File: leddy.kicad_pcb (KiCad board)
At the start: 2 copper layers, 10 parts

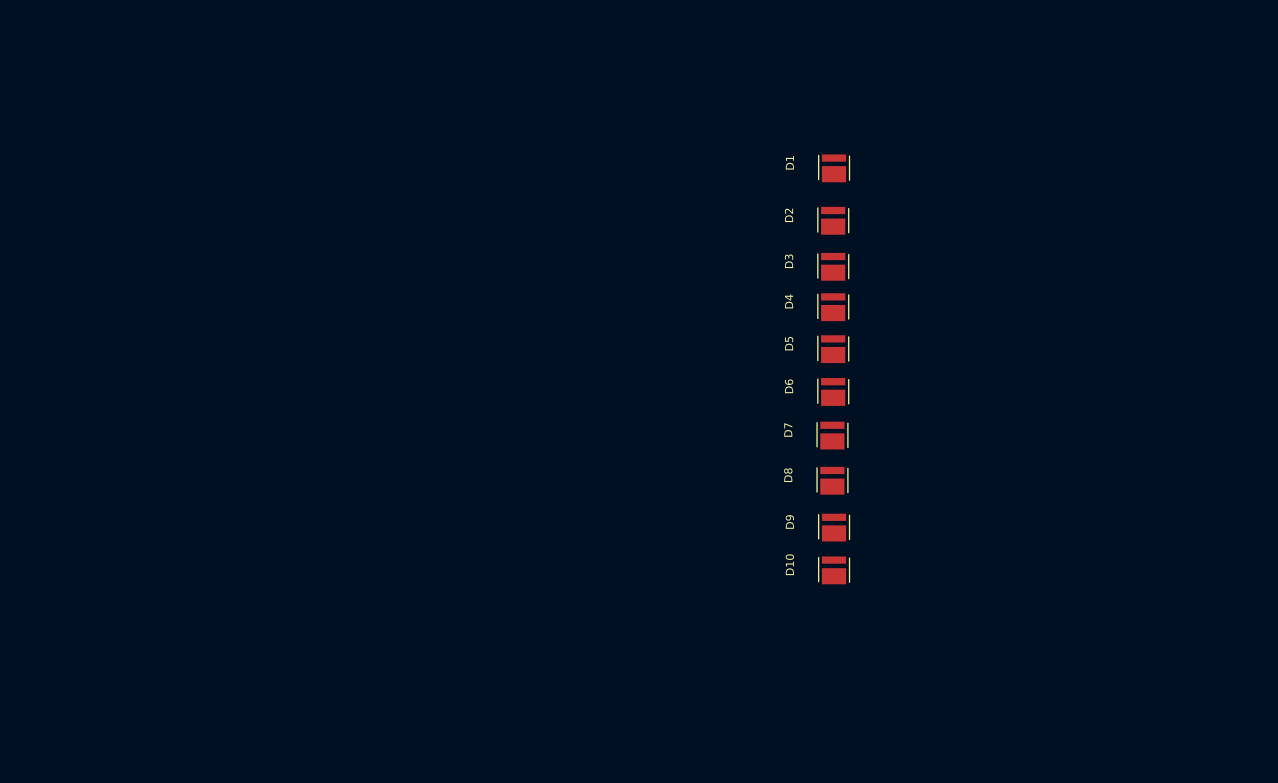
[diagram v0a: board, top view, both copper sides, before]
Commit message: added LED driver IC and added a total of 50 LEDs
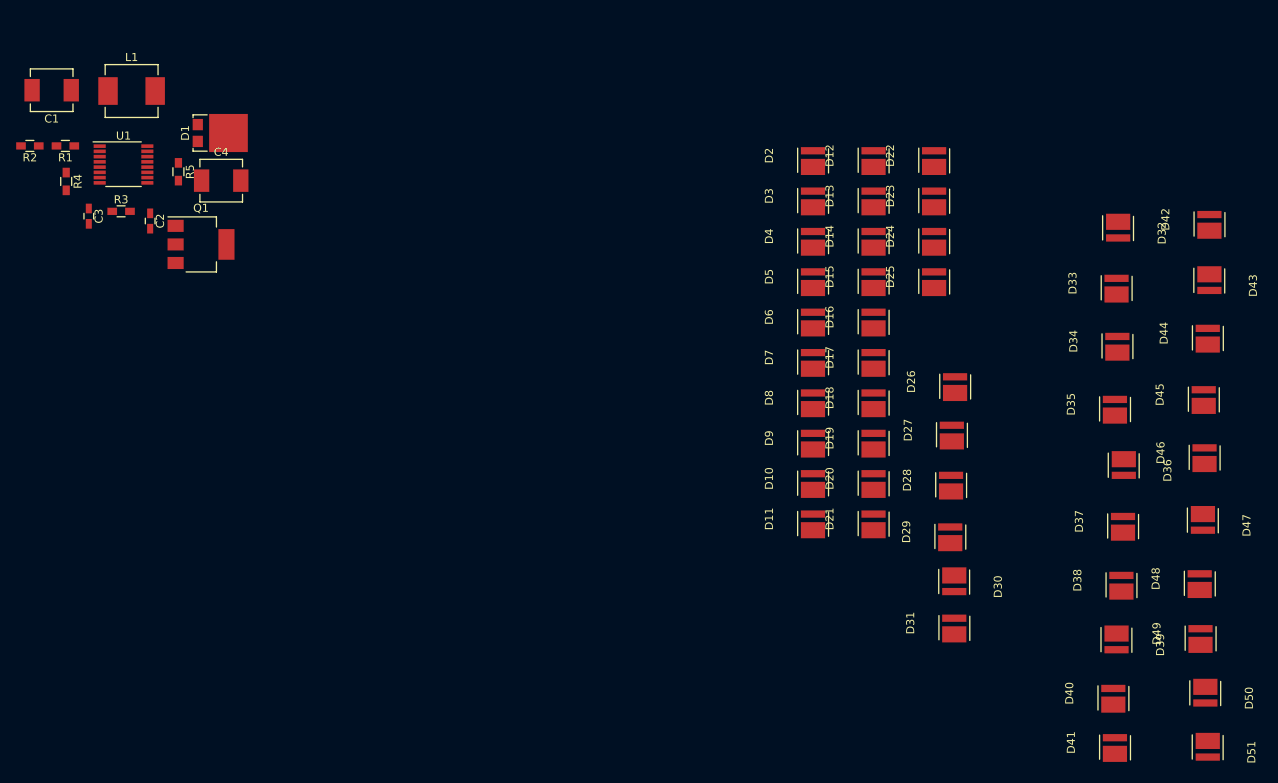
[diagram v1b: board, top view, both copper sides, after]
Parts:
- added C1: 10uF, Inductors_SMD:L_Vishay_IHLP-2020, F.Cu at (70.7, 54.1)
- added C2: 0.1uF, Capacitors_SMD:C_0603_HandSoldering, F.Cu at (82.9, 70.3)
- added C3: 0.1uF, Capacitors_SMD:C_0603_HandSoldering, F.Cu at (75.3, 69.7)
- added C4: 10uF, Inductors_SMD:L_Vishay_IHLP-2020, F.Cu at (91.7, 65.3)
- added D11: LED, lib:LED-3030, F.Cu at (165.0, 107.5)
- added D12: LED, lib:LED-3030, F.Cu at (172.5, 62.5)
- added D13: LED, lib:LED-3030, F.Cu at (172.5, 67.5)
- added D14: LED, lib:LED-3030, F.Cu at (172.5, 72.5)
- added D15: LED, lib:LED-3030, F.Cu at (172.5, 77.5)
- added D16: LED, lib:LED-3030, F.Cu at (172.5, 82.5)
- added D17: LED, lib:LED-3030, F.Cu at (172.5, 87.5)
- added D18: LED, lib:LED-3030, F.Cu at (172.5, 92.5)
- added D19: LED, lib:LED-3030, F.Cu at (172.5, 97.5)
- added D20: LED, lib:LED-3030, F.Cu at (172.5, 102.5)
- added D21: LED, lib:LED-3030, F.Cu at (172.5, 107.5)
- added D22: LED, lib:LED-3030, F.Cu at (180.0, 62.5)
- added D23: LED, lib:LED-3030, F.Cu at (180.0, 67.5)
- added D24: LED, lib:LED-3030, F.Cu at (180.0, 72.5)
- added D25: LED, lib:LED-3030, F.Cu at (180.0, 77.5)
- added D26: LED, lib:LED-3030, F.Cu at (182.6, 90.5)
- added D27: LED, lib:LED-3030, F.Cu at (182.2, 96.5)
- added D28: LED, lib:LED-3030, F.Cu at (182.1, 102.7)
- added D29: LED, lib:LED-3030, F.Cu at (182.0, 109.1)
- added D30: LED, lib:LED-3030, F.Cu at (182.5, 115.3)
- added D31: LED, lib:LED-3030, F.Cu at (182.5, 120.4)
- added D32: LED, lib:LED-3030, F.Cu at (202.8, 71.5)
- added D33: LED, lib:LED-3030, F.Cu at (202.6, 78.3)
- added D34: LED, lib:LED-3030, F.Cu at (202.7, 85.5)
- added D35: LED, lib:LED-3030, F.Cu at (202.4, 93.3)
- added D36: LED, lib:LED-3030, F.Cu at (203.5, 100.9)
- added D37: LED, lib:LED-3030, F.Cu at (203.4, 107.8)
- added D38: LED, lib:LED-3030, F.Cu at (203.2, 115.1)
- added D39: LED, lib:LED-3030, F.Cu at (202.6, 122.5)
- added D40: LED, lib:LED-3030, F.Cu at (202.2, 129.1)
- added D41: LED, lib:LED-3030, F.Cu at (202.4, 135.2)
- added D42: LED, lib:LED-3030, F.Cu at (214.1, 70.4)
- added D43: LED, lib:LED-3030, F.Cu at (214.1, 78.0)
- added D44: LED, lib:LED-3030, F.Cu at (213.9, 84.5)
- added D45: LED, lib:LED-3030, F.Cu at (213.4, 92.1)
- added D46: LED, lib:LED-3030, F.Cu at (213.5, 99.3)
- added D47: LED, lib:LED-3030, F.Cu at (213.3, 107.7)
- added D48: LED, lib:LED-3030, F.Cu at (212.9, 114.9)
- added D49: LED, lib:LED-3030, F.Cu at (213.0, 121.7)
- added D50: LED, lib:LED-3030, F.Cu at (213.6, 129.1)
- added D51: LED, lib:LED-3030, F.Cu at (213.9, 135.8)
- added L1: 10uH, Inductors_SMD:L_Vishay_IHLP-2525, F.Cu at (80.6, 54.2)
- added Q1: ZXMP6A13GTA, TO_SOT_Packages_SMD:SOT-223, F.Cu at (89.2, 73.2)
- added R1: 1M, Resistors_SMD:R_0603_HandSoldering, F.Cu at (72.4, 61.0)
- added R2: 31.6k, Resistors_SMD:R_0603_HandSoldering, F.Cu at (68.0, 61.0)
- added R3: 16.9k, Resistors_SMD:R_0603_HandSoldering, F.Cu at (79.3, 69.1)
- added R4: 16.9k, Resistors_SMD:R_0603_HandSoldering, F.Cu at (72.5, 65.4)
- added R5: 100m, Resistors_SMD:R_0603_HandSoldering, F.Cu at (86.4, 64.2)
- added U1: LT3518EFE#PBF, Housings_SSOP:TSSOP-16_4.4x5mm_Pitch0.65mm, F.Cu at (79.6, 63.3)
- D1: value LED -> SS3P4LHM3_A/H; footprint lib:LED-3030 -> TO_SOT_Packages_SMD:TO-277A
- moved D1 77.0 mm to (90.7, 59.4)
- moved D10 11.0 mm to (165.0, 102.5)
- moved D9 10.7 mm to (165.0, 97.5)
- moved D8 9.90 mm to (165.0, 92.5)
- moved D7 9.31 mm to (165.0, 87.5)
- moved D6 8.96 mm to (165.0, 82.5)
- moved D5 8.67 mm to (165.0, 77.5)
- moved D3 8.48 mm to (165.0, 67.5)
- moved D4 8.48 mm to (165.0, 72.5)
- moved D2 7.81 mm to (165.0, 62.5)
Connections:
- net Net-(D1-Pad1) renamed VLED
- D10 pad 1: GND -> Net-(D10-Pad1)

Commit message: layout almost done
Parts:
- removed D51: LED, lib:LED-3030
- added D100: SS3P4LHM3_A/H, TO_SOT_Packages_SMD:TO-277A, F.Cu at (151.0, 63.0)
- added J1: hole 1, Mounting_Holes:MountingHole_3.2mm_M3_ISO7380_Pad, F.Cu at (128.0, 49.0)
- added J2: hole 1, Mounting_Holes:MountingHole_3.2mm_M3_ISO7380_Pad, F.Cu at (128.0, 106.0)
- added J3: hole 1, Mounting_Holes:MountingHole_3.2mm_M3_ISO7380_Pad, F.Cu at (208.0, 106.0)
- added J4: hole 1, Mounting_Holes:MountingHole_3.2mm_M3_ISO7380_Pad, F.Cu at (208.0, 49.0)
- added J5: umbrella support, Mounting_Holes:MountingHole_6.5mm, F.Cu at (182.0, 78.2)
- added R6: 100m, Resistors_SMD:R_1206_HandSoldering, F.Cu at (139.0, 94.2)
- added R7: 10k, Resistors_SMD:R_0603_HandSoldering, F.Cu at (143.4, 89.1)
- added R8: 100m, Resistors_SMD:R_1206_HandSoldering, F.Cu at (133.4, 89.5)
- added R9: 10k, Resistors_SMD:R_0603_HandSoldering, F.Cu at (139.0, 89.1)
- D1: value SS3P4LHM3_A/H -> LED; footprint TO_SOT_Packages_SMD:TO-277A -> lib:LED-3030
- R2: value 31.6k -> 30.1k
- R3, R4: value 16.9k -> 16.2k
- R5: value 100m -> 10k
- U1: footprint Housings_SSOP:TSSOP-16_4.4x5mm_Pitch0.65mm -> Housings_SSOP:TSSOP-16-1EP_4.4x5mm_Pitch0.65mm
- moved D41 85.3 mm to (201.0, 49.9)
- moved D1 72.9 mm to (163.0, 49.9)
- moved D31 71.1 mm to (191.3, 49.9)
- moved U1 59.9 mm to (139.0, 71.3)
- moved C3 59.5 mm to (134.3, 77.7)
- moved R3 59.5 mm to (138.3, 77.1)
- moved C2 59.5 mm to (141.9, 78.3)
- moved L1 59.5 mm to (139.6, 62.2)
- moved R1 59.5 mm to (131.4, 69.0)
- moved R2 59.5 mm to (127.0, 69.0)
- moved R4 59.5 mm to (131.5, 73.4)
- moved R5 59.5 mm to (145.4, 72.2)
- moved C1 59.5 mm to (129.7, 62.1)
- moved C4 59.5 mm to (150.7, 73.3)
- moved Q1 59.5 mm to (148.2, 81.2)
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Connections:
- D1 pad 1: VLED -> Net-(D1-Pad1)
- D1 pad 2: Net-(D1-Pad2) -> VLED
- D10 pad 1: Net-(D10-Pad1) -> GND
- D11 pad 1: GND -> Net-(D11-Pad1)
- D11 pad 2: Net-(D10-Pad1) -> VLED
- D12 pad 2: VLED -> Net-(D11-Pad1)
- D2 pad 2: VLED -> Net-(D1-Pad1)
- D20 pad 1: Net-(D20-Pad1) -> GND
- D21 pad 1: GND -> Net-(D21-Pad1)
- D21 pad 2: Net-(D20-Pad1) -> VLED
- D22 pad 2: VLED -> Net-(D21-Pad1)
- D30 pad 1: Net-(D30-Pad1) -> GND
- D31 pad 1: GND -> Net-(D31-Pad1)
- D31 pad 2: Net-(D30-Pad1) -> VLED
- D32 pad 2: VLED -> Net-(D31-Pad1)
- D40 pad 1: Net-(D40-Pad1) -> GND
- D41 pad 1: GND -> Net-(D41-Pad1)
- D41 pad 2: Net-(D40-Pad1) -> VLED
- D42 pad 2: VLED -> Net-(D41-Pad1)
- D50 pad 1: Net-(D50-Pad1) -> GND
- L1 pad 2: Net-(D1-Pad2) -> Net-(D100-Pad2)
- R3 pad 2: Net-(R3-Pad2) -> CTRL
- R5 pad 1: VLED -> CTRL
- R5 pad 2: Net-(Q1-Pad3) -> GND
- U1 pad 10: Net-(R3-Pad2) -> CTRL
- U1 pad 12: Net-(Q1-Pad3) -> Net-(R1-Pad2)
- U1 pad 15: Net-(D1-Pad2) -> Net-(D100-Pad2)
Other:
- board outline added: 88 x 65 mm

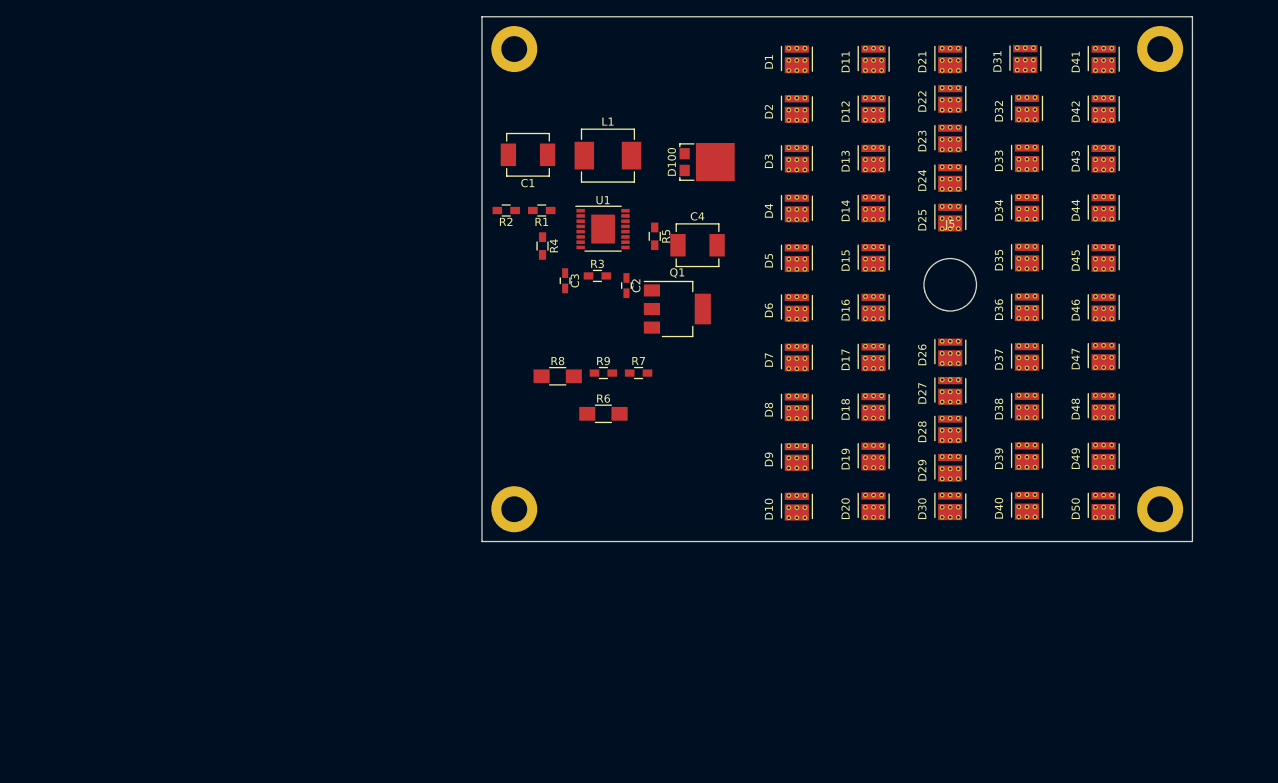
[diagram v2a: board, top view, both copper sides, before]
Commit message: added the LED intensity selection circuit
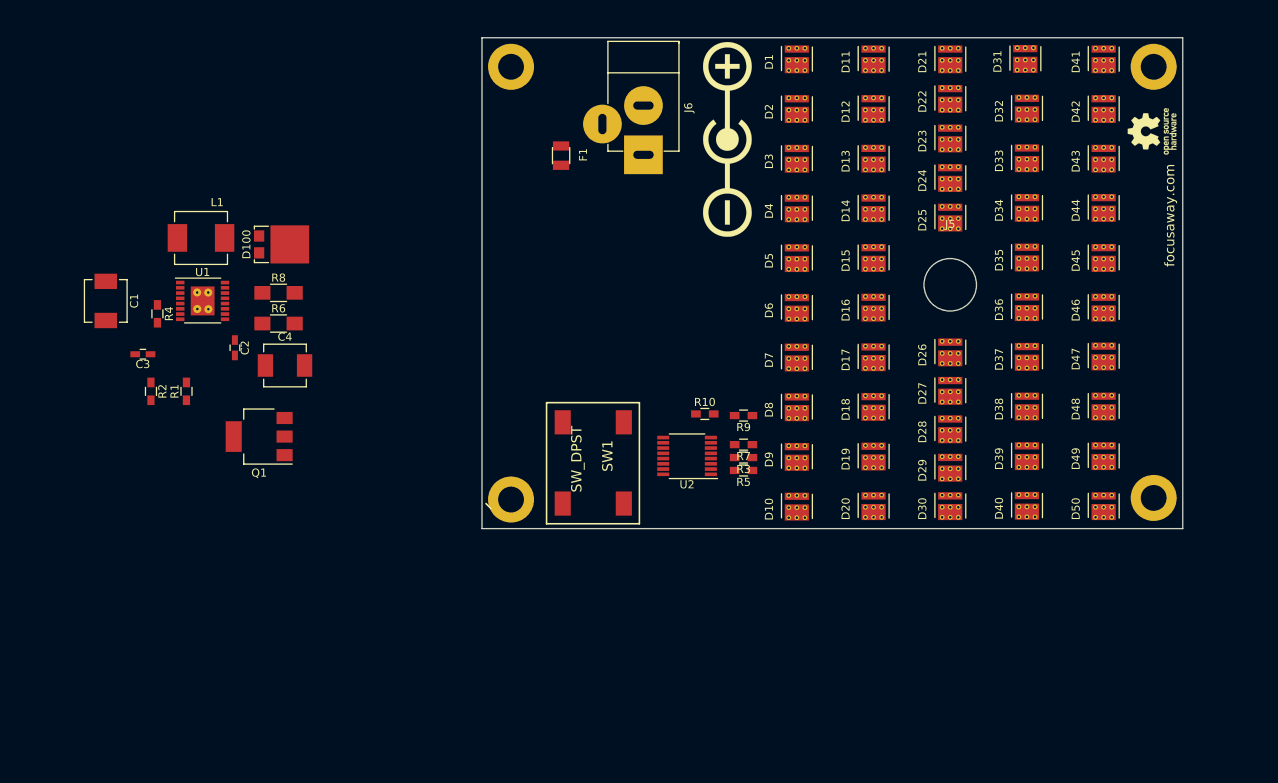
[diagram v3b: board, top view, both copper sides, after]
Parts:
- added F1: Fuse, Fuse_Holders_and_Fuses:Fuse_SMD1206_Reflow, F.Cu at (133.8, 62.2)
- added J6: BARREL_JACK, Connectors:JACK_ALIM, F.Cu at (144.0, 62.1)
- added J7: OPEN HARDWARE, Symbols:OSHW-Logo_5.7x6mm_SilkScreen, F.Cu at (207.0, 59.2)
- added J8: label_power-in, Symbols:Polarity_Center_Positive_6mm_SilkScreen, F.Cu at (154.4, 60.2)
- added R10: 16.2k, Resistors_SMD:R_0603_HandSoldering, F.Cu at (151.6, 94.2)
- added SW1: SW_DPST, lib:sw_push4p, F.Cu at (137.0, 99.8)
- added U2: 74HC4017PW, Housings_SSOP:TSSOP-16_4.4x5mm_Pitch0.65mm, F.Cu at (149.4, 99.4)
- R5: value 10k -> 20k
- R7: value 10k -> 30k
- R9: value 10k -> 40k
- U1: footprint Housings_SSOP:TSSOP-16-1EP_4.4x5mm_Pitch0.65mm -> lib:TSSOP-16-1EP_4.4x5mm_Pitch0.65mm-thermal
- moved C1 55.3 mm to (77.4, 80.2), turned to 270 degrees
- moved Q1 54.2 mm to (96.4, 97.0), turned to 180 degrees
- moved D100 53.7 mm to (98.3, 73.2)
- moved C4 53.2 mm to (99.6, 88.2)
- moved C3 53.1 mm to (82.0, 86.8), turned to 180 degrees
- moved L1 51.4 mm to (89.2, 72.4)
- moved U1 50.4 mm to (89.4, 80.2)
- moved R1 49.4 mm to (87.4, 91.4), turned to 90 degrees
- moved R2 49.4 mm to (83.0, 91.4), turned to 270 degrees
- moved C2 49.1 mm to (93.4, 86.0)
- moved R4 48.4 mm to (83.8, 81.8)
- moved R6 41.8 mm to (98.8, 83.0)
- moved R8 36.1 mm to (98.8, 79.2)
- moved R5 31.0 mm to (156.4, 101.2), turned to 180 degrees
- moved R3 28.9 mm to (156.4, 99.6), turned to 180 degrees
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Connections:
- R3 pad 1: Net-(R3-Pad1) -> CTRL
- R3 pad 2: CTRL -> Net-(R3-Pad2)
- R5 pad 2: GND -> Net-(R5-Pad2)
- R7 pad 2: GND -> Net-(R7-Pad2)
- R9 pad 2: GND -> Net-(R9-Pad2)
- U1 pad 5: Net-(R3-Pad1) -> Vref
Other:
- board size 88 x 65 mm -> 86.8 x 60.8 mm
- copper layers 2 -> 4
- board text added: "focusaway.com"
